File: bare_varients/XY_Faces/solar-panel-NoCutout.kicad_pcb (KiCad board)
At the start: 4 copper layers, 83 x 98 mm, 32 parts, among them J1 CON-5040500591, J2 Conn_01x01, J3 Conn_01x01, J4 Conn_01x01, J5 Conn_01x01, U1 VEML7700, U2 MCP9808_DFN, U3 DRV2605LDGS

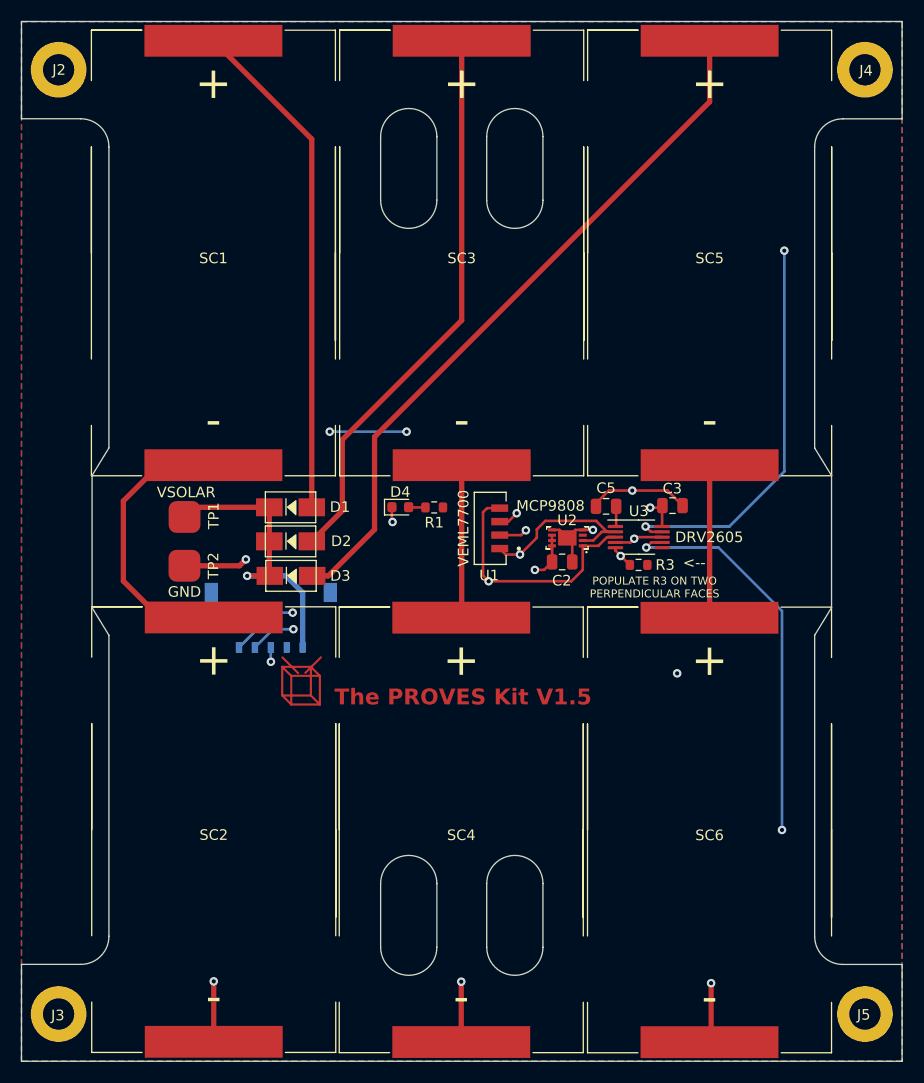
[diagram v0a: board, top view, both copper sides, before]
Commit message: Updated XY Board with Pleiades Five
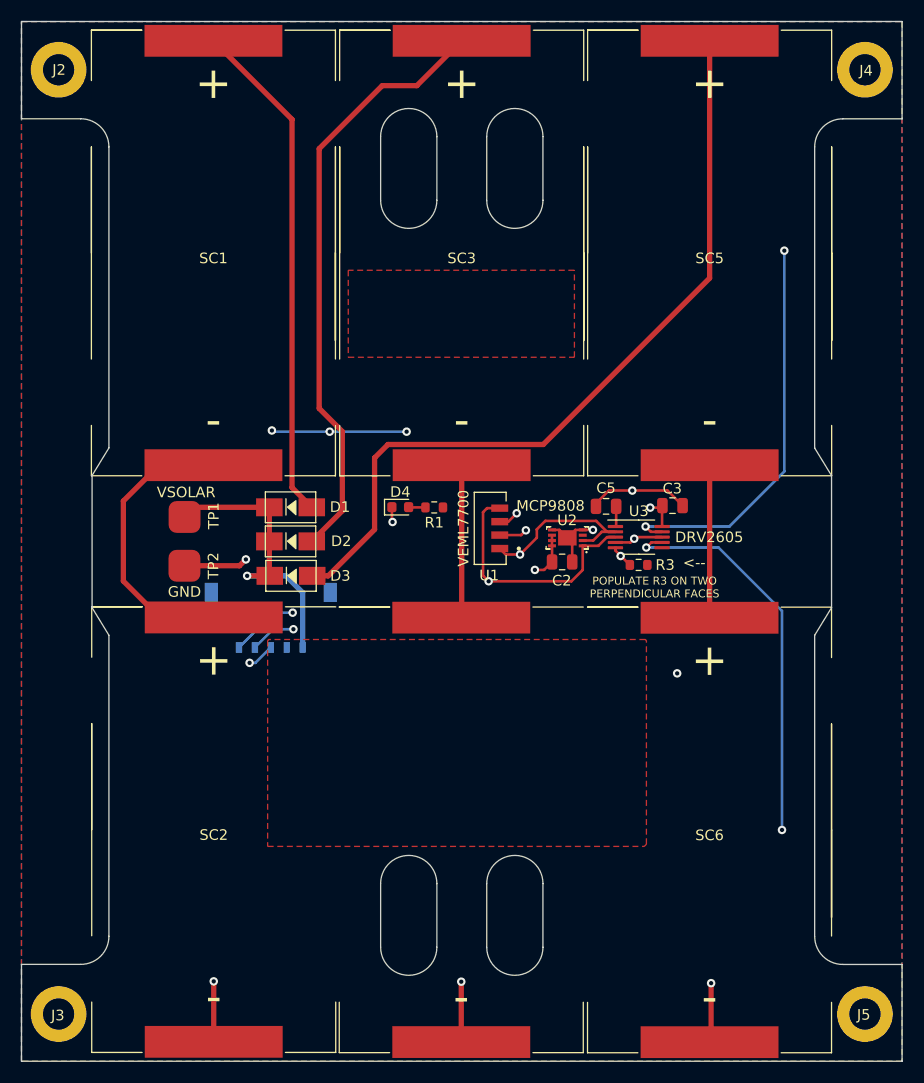
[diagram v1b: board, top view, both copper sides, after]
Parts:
- removed the G*** at (145.3, 92.7)
- removed the G*** at (157.7, 101.6)
- added G***: LOGO, LOGO, F.Cu at (145.2, 139.3)
- added G***: LOGO, LOGO, F.Cu at (157.3, 129.9)
- G***: moved to B.Cu
- moved G*** 47.0 mm to (144.7, 89.6), turned to 180 degrees
- moved G*** 43.2 mm to (151.2, 134.9)
- moved G*** 40.0 mm to (157.5, 139.6)
- moved G*** 38.2 mm to (134.2, 134.3)
- moved G*** 33.6 mm to (145.4, 129.7)
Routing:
- net Net-(D3-Pad2): track 66.8 -> 75.4 mm
- net +3V3: track 19.8 -> 26.5 mm, vias 5 -> 6
- net Net-(D2-Pad2): track 53.0 -> 56.7 mm
- added copper zone on F.Cu, net (none)
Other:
- board text added: "PROVES XY SOLAR: YEARLING KIT V1.5 AMANDA EWING, NICOLE MAGGARD"
- board text removed: "PROVES XY SOLAR: YEARLING KIT AMANDA EWING, NICOLE MAGGARD"

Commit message: Updated Logos
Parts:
- moved G*** 0.50 mm to (150.9, 135.3)

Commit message: Updated Logos
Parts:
- moved G*** 0.32 mm to (157.2, 130.2)

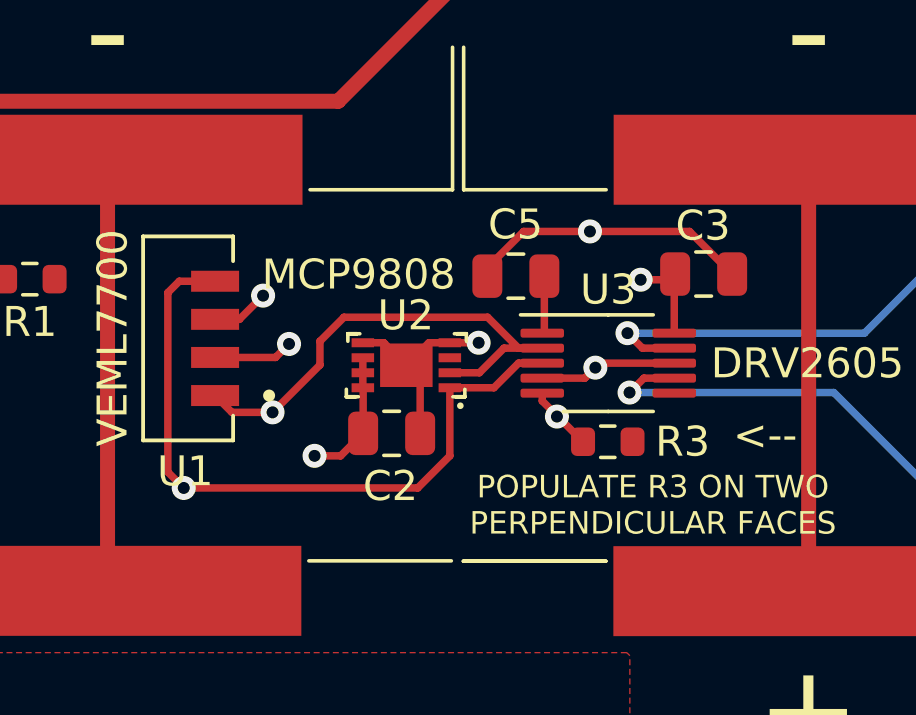
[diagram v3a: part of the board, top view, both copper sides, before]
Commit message: Adjusted Solar Board
Changed temperature sensor footprint from DFM to MSOP
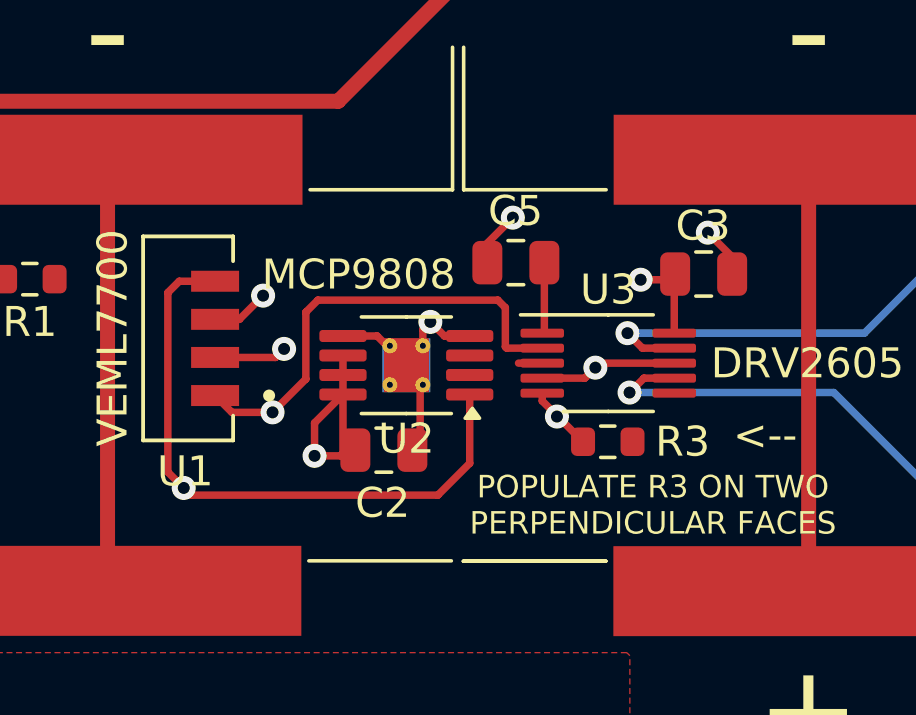
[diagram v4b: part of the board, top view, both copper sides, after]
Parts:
- U2: footprint SolarPanelBoards:MCP9808-NoLeadPackage -> Package_SO:MSOP-8-1EP_3x3mm_P0.65mm_EP1.5x1.8mm_ThermalVias
- moved C2 0.62 mm to (153.7, 117.2)
- moved C5 0.45 mm to (158.1, 111.0)
- turned U2 to 180 degrees
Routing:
- net GND: track 47.4 -> 43.2 mm, vias 9 -> 10
- net +3V3: track 26.5 -> 28.4 mm
- net SDA: track 49.6 -> 47.7 mm
